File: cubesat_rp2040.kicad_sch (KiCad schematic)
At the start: 36 parts, among them J1 FTSH-105-01-L-DV-007, J2 Conn_01x02, SW1 SW_Push, U1 RP2040, U2 W25Q128JVS, U3 AMS1117-3.3, Y1 12.00 MHz

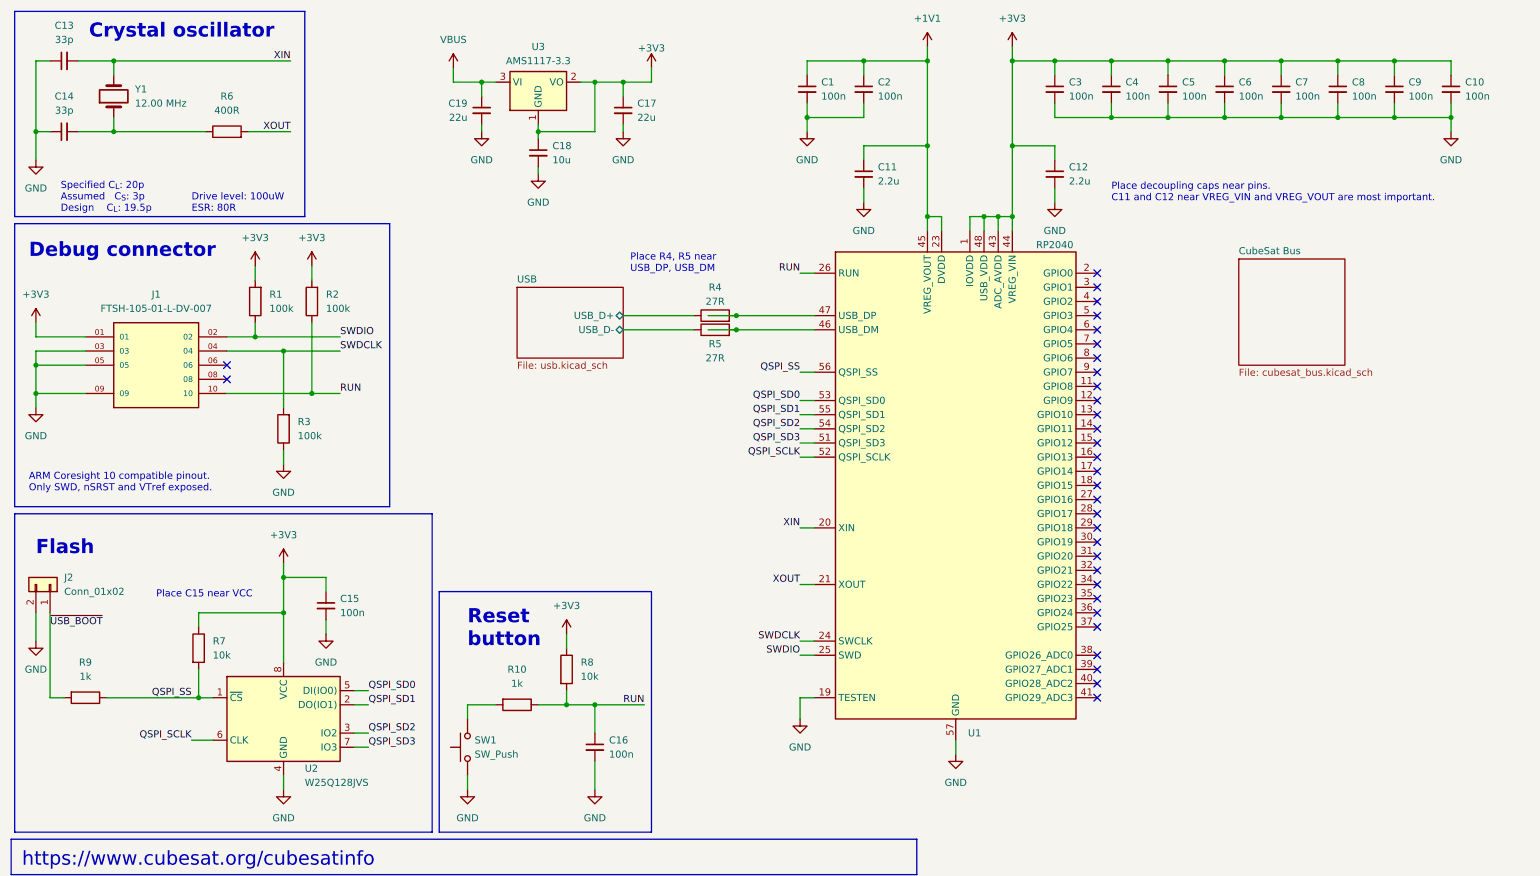
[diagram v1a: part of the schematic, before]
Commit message: break out subcircuits, add switching regulator
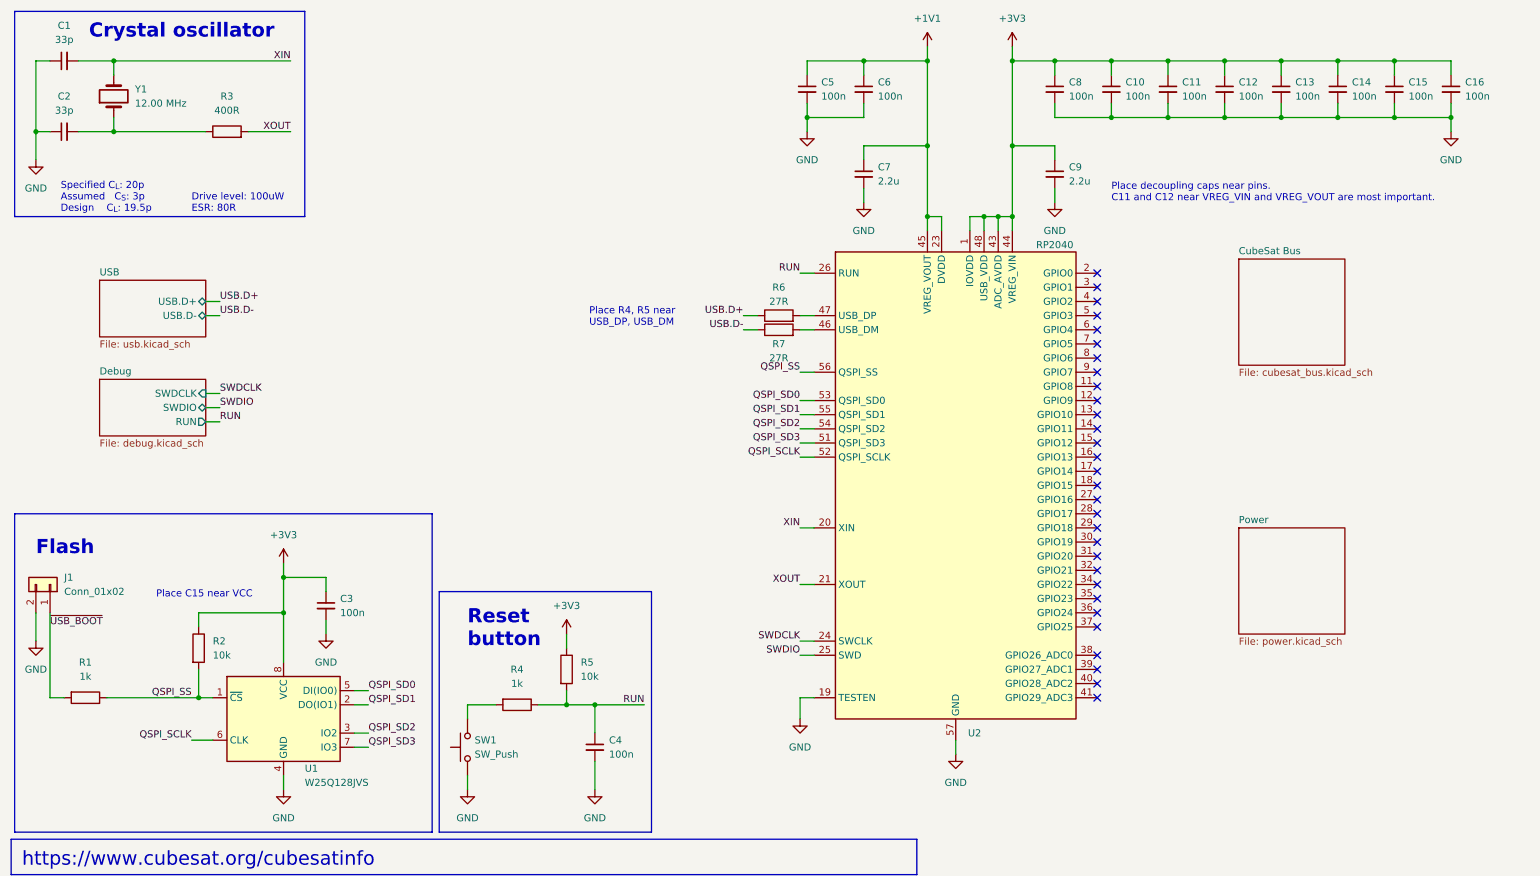
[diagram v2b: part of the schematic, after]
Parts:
- removed C17, C19: 22u, Capacitor_SMD:C_1206_3216Metric, symbol Device:C_Small
- removed C18: 10u, Capacitor_SMD:C_1206_3216Metric, symbol Device:C_Small
- removed J1: FTSH-105-01-L-DV-007, cubesat_rp2040:SAMTEC_FTSH-105-01-L-DV-007, symbol cubesat_rp2040:FTSH-105-01-L-DV-007
- removed R1, R2, R3: 100k, Resistor_SMD:R_1206_3216Metric, symbol Device:R
- removed U3: AMS1117-3.3, Package_TO_SOT_SMD:SOT-223-3_TabPin2, symbol Regulator_Linear:AMS1117-3.3
- renumbered C13 to C1, C4 to C10, C5 to C11, C6 to C12, C7 to C13, C8 to C14, C9 to C15, C10 to C16, C14 to C2, C15 to C3, C16 to C4, C1 to C5, C2 to C6, C11 to C7, C3 to C8, C12 to C9, J2 to J1, R9 to R1, R7 to R2, R6 to R3, R10 to R4, R8 to R5, R4 to R6, R5 to R7, U2 to U1, U1 to U2
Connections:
- net USB/USB_D+ renamed USB.D+
- net USB/USB_D- renamed USB.D-
- no-connect marks 32 -> 30
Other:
- added sheet Debug (debug.kicad_sch)
- added sheet Power (power.kicad_sch)
- sheet USB ports: added USB.D+, USB.D-; removed USB_D+, USB_D-
- note removed: "ARM Coresight 10 compatible pinout. Only SWD, nSRST and VTref exposed."
- note removed: "Debug connector"
- moved on the sheet: R6, R7

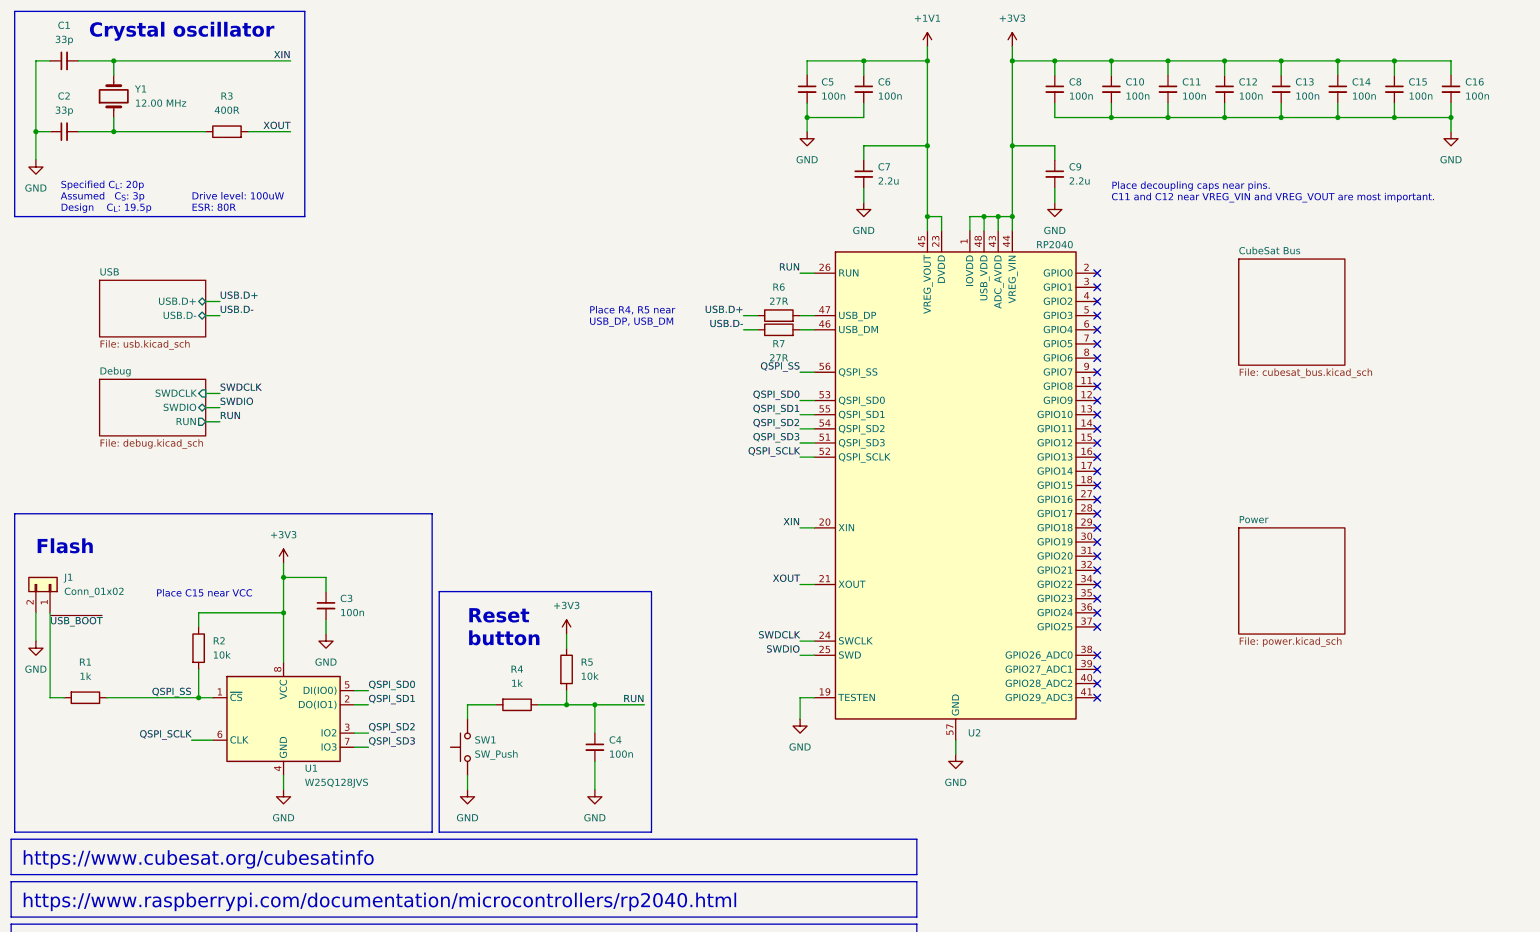
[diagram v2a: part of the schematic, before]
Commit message: Block diagram
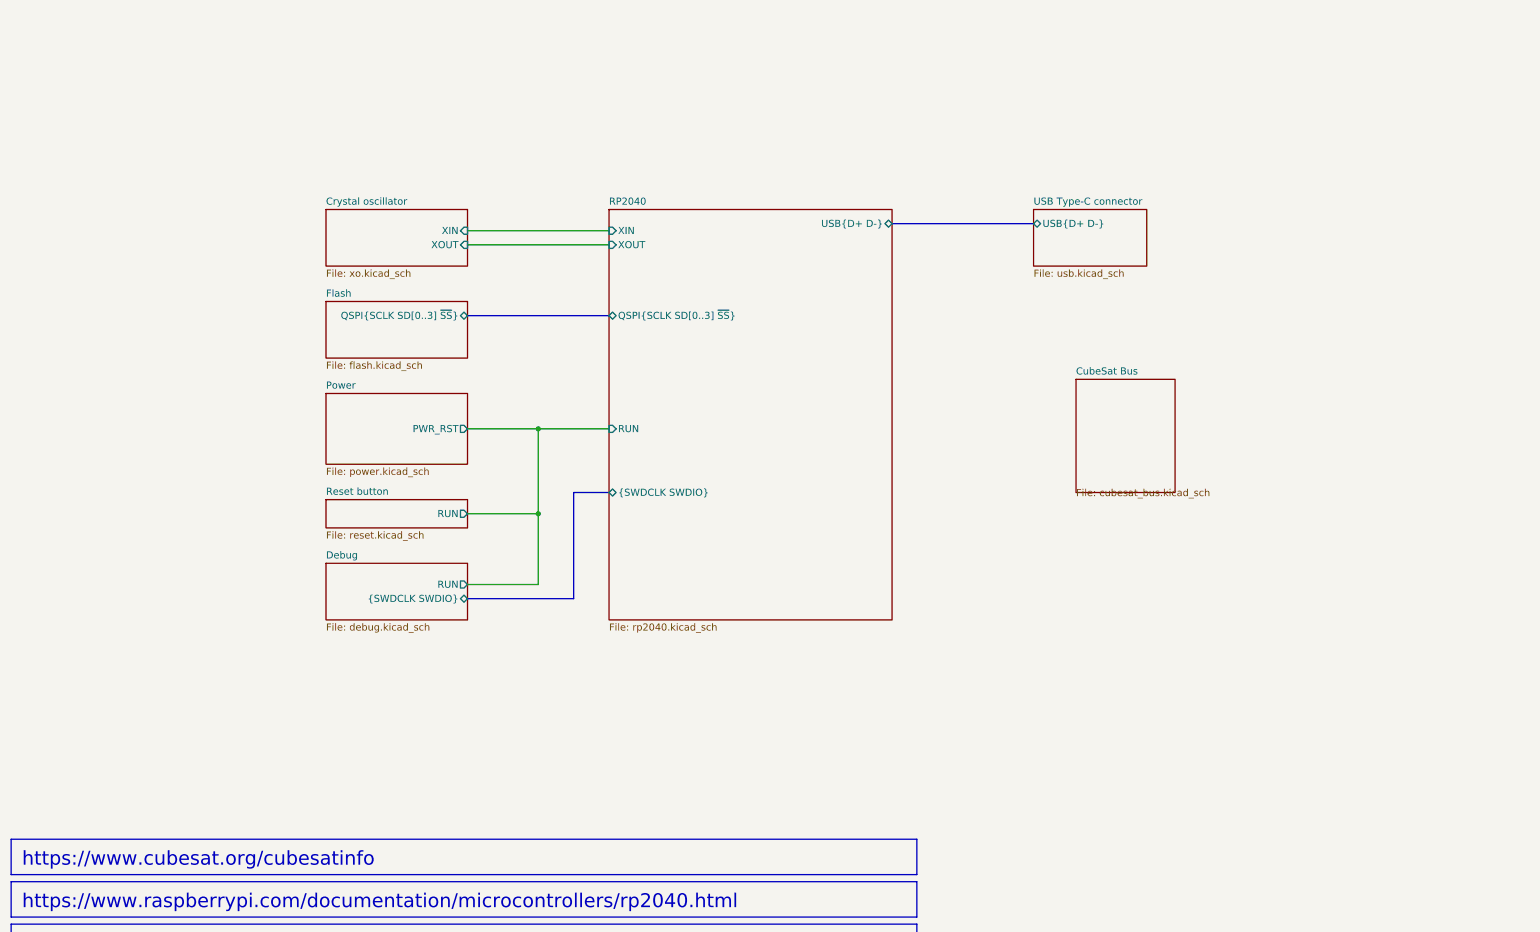
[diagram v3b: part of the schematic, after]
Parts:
- removed C1, C2: 33p, Capacitor_SMD:C_1206_3216Metric, symbol Device:C_Small
- removed C10, C11, C12, C13, C14, C15, C16, C3, C4, C6, C8: 100n, Capacitor_SMD:C_1206_3216Metric, symbol Device:C_Small
- removed C5: 100n, Button_Switch_SMD:SW_Push_1P1T_NO_CK_KMR2, symbol Device:C_Small
- removed C7, C9: 2.2u, Capacitor_SMD:C_1206_3216Metric, symbol Device:C_Small
- removed J1: Conn_01x02, Connector_PinHeader_2.54mm:PinHeader_1x02_P2.54mm_Horizontal, symbol Connector_Generic:Conn_01x02
- removed R1, R4: 1k, Resistor_SMD:R_1206_3216Metric, symbol Device:R
- removed R2, R5: 10k, Resistor_SMD:R_1206_3216Metric, symbol Device:R
- removed R3: 400R, Resistor_SMD:R_1206_3216Metric, symbol Device:R
- removed R6, R7: 27R, Resistor_SMD:R_1206_3216Metric, symbol Device:R
- removed SW1: SW_Push, Button_Switch_SMD:SW_Push_1P1T_NO_CK_KMR2, symbol Switch:SW_Push
- removed U1: W25Q128JVS, Package_SO:SOIC-8_5.23x5.23mm_P1.27mm, symbol cubesat_rp2040:W25Q128JVS
- removed U2: RP2040, Package_DFN_QFN:QFN-56-1EP_7x7mm_P0.4mm_EP3.2x3.2mm, symbol cubesat_rp2040:RP2040
- removed Y1: 12.00 MHz, symbol Device:Crystal
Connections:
- no-connect marks 30 -> 0
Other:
- sheet USB renamed USB Type-C connector
- added sheet Crystal oscillator (xo.kicad_sch)
- added sheet Flash (flash.kicad_sch)
- added sheet RP2040 (rp2040.kicad_sch)
- added sheet Reset button (reset.kicad_sch)
- sheet Debug ports: added {SWDCLK SWDIO}; removed SWDCLK, SWDIO
- sheet Power ports: added PWR_RST; removed none
- sheet USB Type-C connector ports: added USB{D+ D-}; removed USB.D+, USB.D-
- note removed: "Crystal oscillator"
- note removed: "Drive level: 100uW ESR: 80R"
- note removed: "Flash"
- note removed: "Place C15 near VCC"
- note removed: "Place R4, R5 near USB_DP, USB_DM"
- note removed: "Place decoupling caps near pins. C11 and C12 near VREG_VIN and VREG_VOUT are most important."
- note removed: "Reset button"
- note removed: "Specified C_{L}: 20p Assumed C_{S}: 3p Design C_{L}: 19.5p"

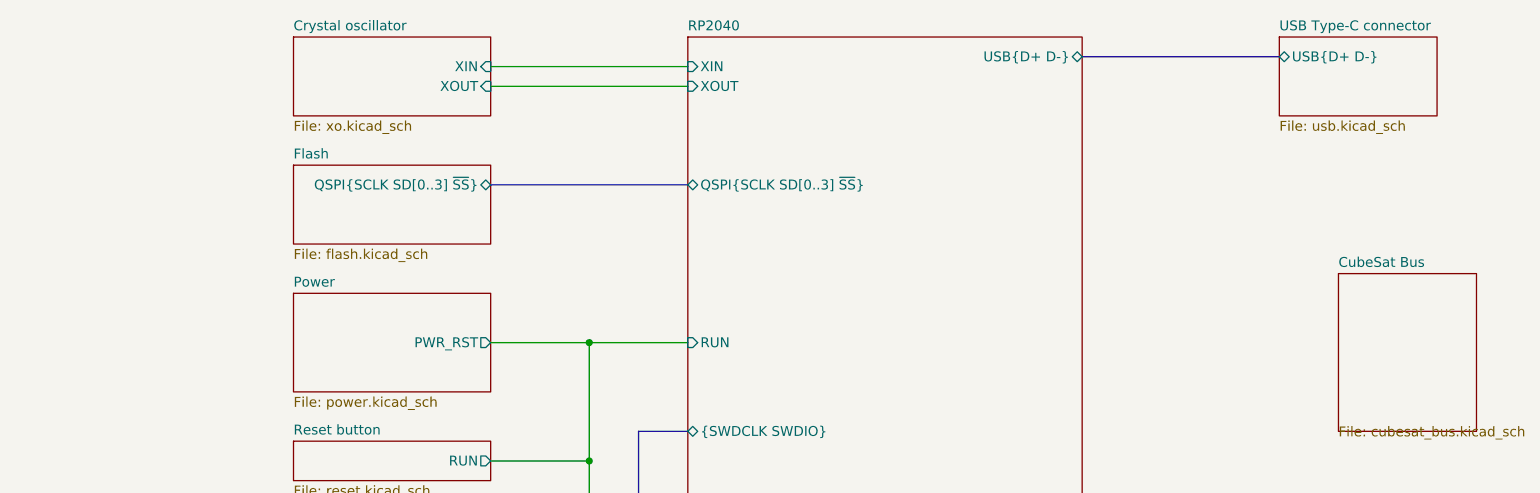
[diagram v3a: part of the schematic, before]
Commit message: Complete power regulator schematics
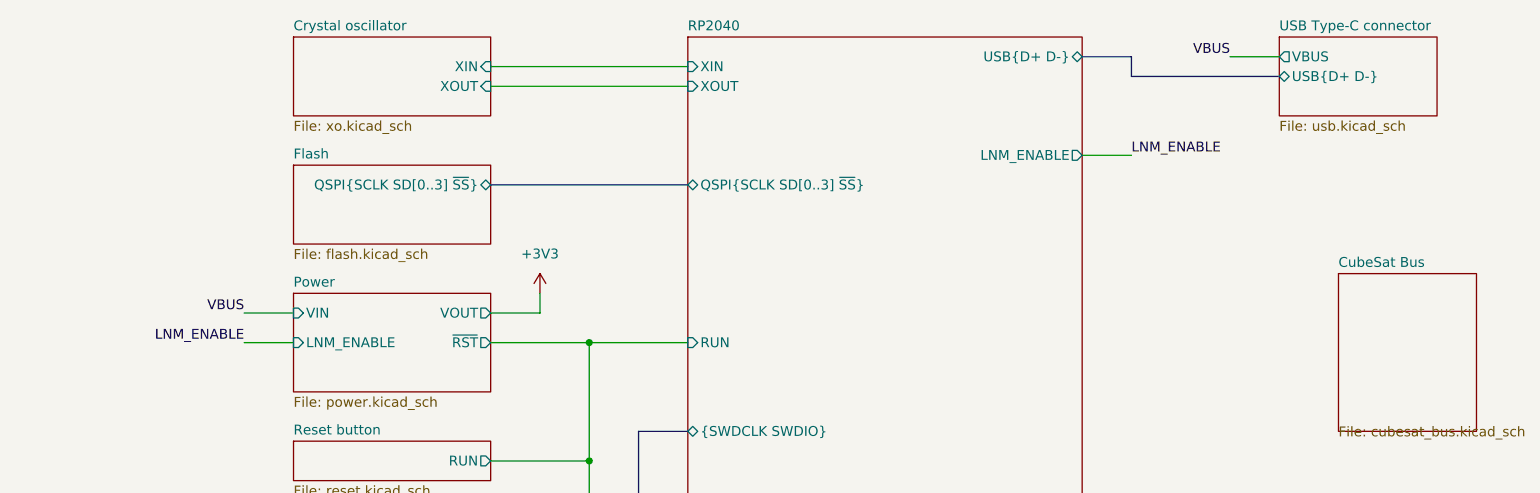
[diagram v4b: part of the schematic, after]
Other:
- sheet Power ports: added LNM_ENABLE, VIN, VOUT, ~{RST}; removed PWR_RST
- sheet RP2040 ports: added LNM_ENABLE; removed none
- sheet USB Type-C connector ports: added VBUS; removed none
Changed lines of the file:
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@@
+		)
+	)
+	(bus
+		(pts
+			(xy 177.8 57.15) (xy 171.45 57.15)
+		)
+		(stroke
+			(width 0)
+			(type default)
+		)
+	)
+	(bus
+		(pts
+			(xy 177.8 59.69) (xy 177.8 57.15)
+		)
+		(stroke
+			(width 0)
+			(type default)
+		)
+	)
+	(wire
+		(pts
+			(xy 63.5 93.98) (xy 69.85 93.98)
+		)
+		(stroke
+			(width 0)
+			(type default)
 		)
 	)
@@
 	(wire
 		(pts
+			(xy 101.6 87.63) (xy 101.6 90.17)
+		)
+		(stroke
+			(width 0)
+			(type default)
+		)
+	)
+	(wire
+		(pts
 			(xy 107.95 93.98) (xy 107.95 109.22)
 		)
@@
 	(bus
 		(pts
-			(xy 171.45 57.15) (xy 196.85 57.15)
+			(xy 196.85 59.69) (xy 177.8 59.69)
+		)
+		(stroke
+			(width 0)
+			(type default)
+		)
+	)
+	(wire
+		(pts
+			(xy 190.5 57.15) (xy 196.85 57.15)
+		)
+		(stroke
+			(width 0)
+			(type default)
+		)
+	)
+	(wire
+		(pts
+			(xy 171.45 69.85) (xy 177.8 69.85)
 		)
 		(stroke
@@
 		(pts
 			(xy 114.3 105.41) (xy 120.65 105.41)
+		)
+		(stroke
+			(width 0)
+			(type default)
+		)
+	)
+	(wire
+		(pts
+			(xy 101.6 90.17) (xy 95.25 90.17)
+		)
+		(stroke
+			(width 0)
+			(type default)
+		)
+	)
+	(wire
+		(pts
+			(xy 63.5 90.17) (xy 69.85 90.17)
 		)
 		(stroke
@@
 		)
 	)
+	(label "LNM_ENABLE"
+		(at 63.5 93.98 180)
+		(fields_autoplaced yes)
+		(effects
+			(font
+				(size 1.27 1.27)
+			)
+			(justify right bottom)
+		)
+	)
+	(label "LNM_ENABLE"
+		(at 177.8 69.85 0)
+		(fields_autoplaced yes)
+		(effects
+			(font
+				(size 1.27 1.27)
+			)
+			(justify left bottom)
+		)
+	)
+	(label "VBUS"
+		(at 63.5 90.17 180)
+		(fields_autoplaced yes)
+		(effects
+			(font
+				(size 1.27 1.27)
+			)
+			(justify right bottom)
+		)
+	)
+	(label "VBUS"
+		(at 190.5 57.15 180)
+		(fields_autoplaced yes)
+		(effects
+			(font
+				(size 1.27 1.27)
+			)
+			(justify right bottom)
+		)
+	)
+	(symbol
+		(lib_id "power:+3V3")
+		(at 101.6 87.63 0)
+		(unit 1)
+		(exclude_from_sim no)
+		(in_bom yes)
+		(on_board yes)
+		(dnp no)
+		(fields_autoplaced yes)
+		(property "Reference" "#PWR07"
+			(at 101.6 91.44 0)
+			(effects
+				(font
+					(size 1.27 1.27)
+				)
+				(hide yes)
+			)
+		)
+		(property "Value" "+3V3"
+			(at 101.6 82.55 0)
+			(effects
+				(font
+					(size 1.27 1.27)
+				)
+			)
+		)
+		(property "Footprint" ""
+			(at 101.6 87.63 0)
+			(effects
+				(font
+					(size 1.27 1.27)
+				)
+				(hide yes)
+			)
+		)
+		(property "Datasheet" ""
+			(at 101.6 87.63 0)
+			(effects
+				(font
+					(size 1.27 1.27)
+				)
+				(hide yes)
+			)
+		)
+		(property "Description" "Power symbol creates a global label with name \"+3V3\""
+			(at 101.6 87.63 0)
+			(effects
+				(font
+					(size 1.27 1.27)
+				)
+				(hide yes)
+			)
+		)
+		(pin "1"
+		)
+		(instances
+			(project "cubesat_rp2040"
+				(path "/5511013b-c214-40ba-8960-f470f52474f8"
+					(reference "#PWR07")
+					(unit 1)
+				)
+			)
+		)
+	)
 	(sheet
 		(at 204.47 85.09)
@@
 			)
 		)
+		(pin "LNM_ENABLE" output
+			(at 171.45 69.85 0)
+			(effects
+				(font
+					(size 1.27 1.27)
+				)
+				(justify right)
+			)
+		)
 		(instances
 			(project "cubesat_rp2040"
@@
 		)
 		(pin "USB{D+ D-}" bidirectional
+			(at 196.85 59.69 180)
+			(effects
+				(font
+					(size 1.27 1.27)
+				)
+				(justify left)
+			)
+		)
+		(pin "VBUS" output
 			(at 196.85 57.15 180)
 			(effects
@@
 			)
 		)
-		(pin "PWR_RST" output
+		(pin "VOUT" output
+			(at 95.25 90.17 0)
+			(effects
+				(font
+					(size 1.27 1.27)
+				)
+				(justify right)
+			)
+		)
+		(pin "~{RST}" output
 			(at 95.25 93.98 0)
 			(effects
@@
 			)
 		)
+		(pin "LNM_ENABLE" input
+			(at 69.85 93.98 180)
+			(effects
+				(font
+					(size 1.27 1.27)
+				)
+				(justify left)
+			)
+		)
+		(pin "VIN" input
+			(at 69.85 90.17 180)
+			(effects
+				(font
+					(size 1.27 1.27)
+				)
+				(justify left)
+			)
+		)
